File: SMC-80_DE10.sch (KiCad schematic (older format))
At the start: 19 parts, among them J1 IDE, J2 Port A, J3 Arduino1, J4 DE10-Lite GPIO, J5 Arduino2

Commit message: Renamed to SMC-80 DE10, new layout
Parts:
- C1: symbol de10-lite-ram-rom-ide-rescue:C_Small-Device-sbc_z80-rescue-THS-80-rescue-de10-lite-ram-rom-rescue -> SMC-80_DE10-rescue:C_Small-Device-sbc_z80-rescue-THS-80-rescue-de10-lite-ram-rom-rescue
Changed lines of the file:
@@
 NoConn ~ 2400 1250
 $Comp
-L de10-lite-ram-rom-ide-rescue:C_Small-Device-sbc_z80-rescue-THS-80-rescue-de10-lite-ram-rom-rescue C?
+L SMC-80_DE10-rescue:C_Small-Device-sbc_z80-rescue-THS-80-rescue-de10-lite-ram-rom-rescue C?
 U 1 1 5D65939B
 P 3300 2050
@@
 $EndComp
 $Comp
-L de10-lite-ram-rom-ide-rescue:GND-power-sbc_z80-rescue-THS-80-rescue-de10-lite-ram-rom-rescue #PWR06
+L SMC-80_DE10-rescue:GND-power-sbc_z80-rescue-THS-80-rescue-de10-lite-ram-rom-rescue #PWR06
 U 1 1 5D65A340
 P 3300 2150

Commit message: rotated layout
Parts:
- removed C1: 100nF, Capacitor_SMD:C_0603_1608Metric_Pad1.05x0.95mm_HandSolder, symbol SMC-80_DE10-rescue:C_Small-Device-sbc_z80-rescue-THS-80-rescue-de10-lite-ram-ro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
- removed D1: GRN, LED_SMD:LED_0603_1608Metric_Pad1.05x0.95mm_HandSolder, symbol Device:LED
- removed J1: IDE, Connector_PinHeader_2.54mm:PinHeader_2x20_P2.54mm_Horizontal, symbol Connector_Generic:Conn_02x20_Odd_Even
- removed J2: Port A, Connector_PinHeader_2.54mm:PinHeader_1x06_P2.54mm_Vertical, symbol Connector_Generic:Conn_01x06
- removed JP1: IDE PWR, Connector_PinHeader_2.54mm:PinHeader_1x02_P2.54mm_Vertical, symbol Device:Jumper_NC_Small
- removed R1, R2, R3, R4: 10K, Resistor_SMD:R_0603_1608Metric_Pad1.05x0.95mm_HandSolder, symbol Device:R_Small
- removed R5: 1K, Resistor_SMD:R_0603_1608Metric_Pad1.05x0.95mm_HandSolder, symbol Device:R_Small
- removed R6, R8: 100K, Resistor_SMD:R_0603_1608Metric_Pad1.05x0.95mm_HandSolder, symbol Device:R_Small
- removed RN1: 2K2, Resistor_SMD:R_Cat16-4, symbol Device:R_Pack04
- renumbered C2 to C1, D2 to D1, J3 to J1, J4 to J2, J5 to J3, R7 to R1
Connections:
- net labels removed: IDE_~CE~, RX, TX, ~ACTIVE, ~CTS, ~RTS
- wire segments 156 -> 88
- no-connect marks 22 -> 14
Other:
- note removed: "AB5"
- note removed: "AB6"
- note removed: "AB7"
- note removed: "AB8"
- note removed: "IDE Activity"
- moved on the sheet: C1, D1, J1, J2, J3, R1

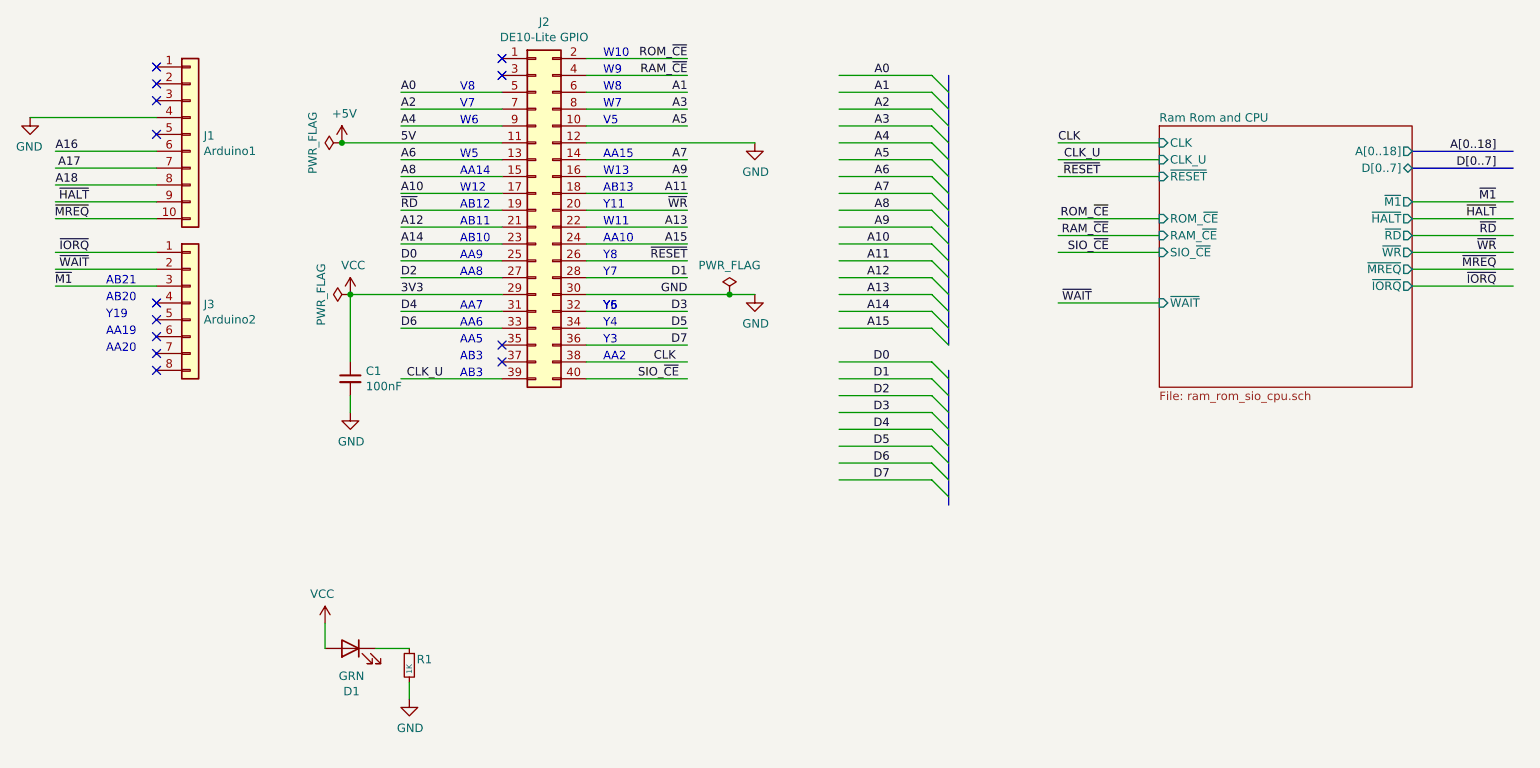
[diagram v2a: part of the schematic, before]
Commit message: Routing completed, fixed RAM/ROM paging
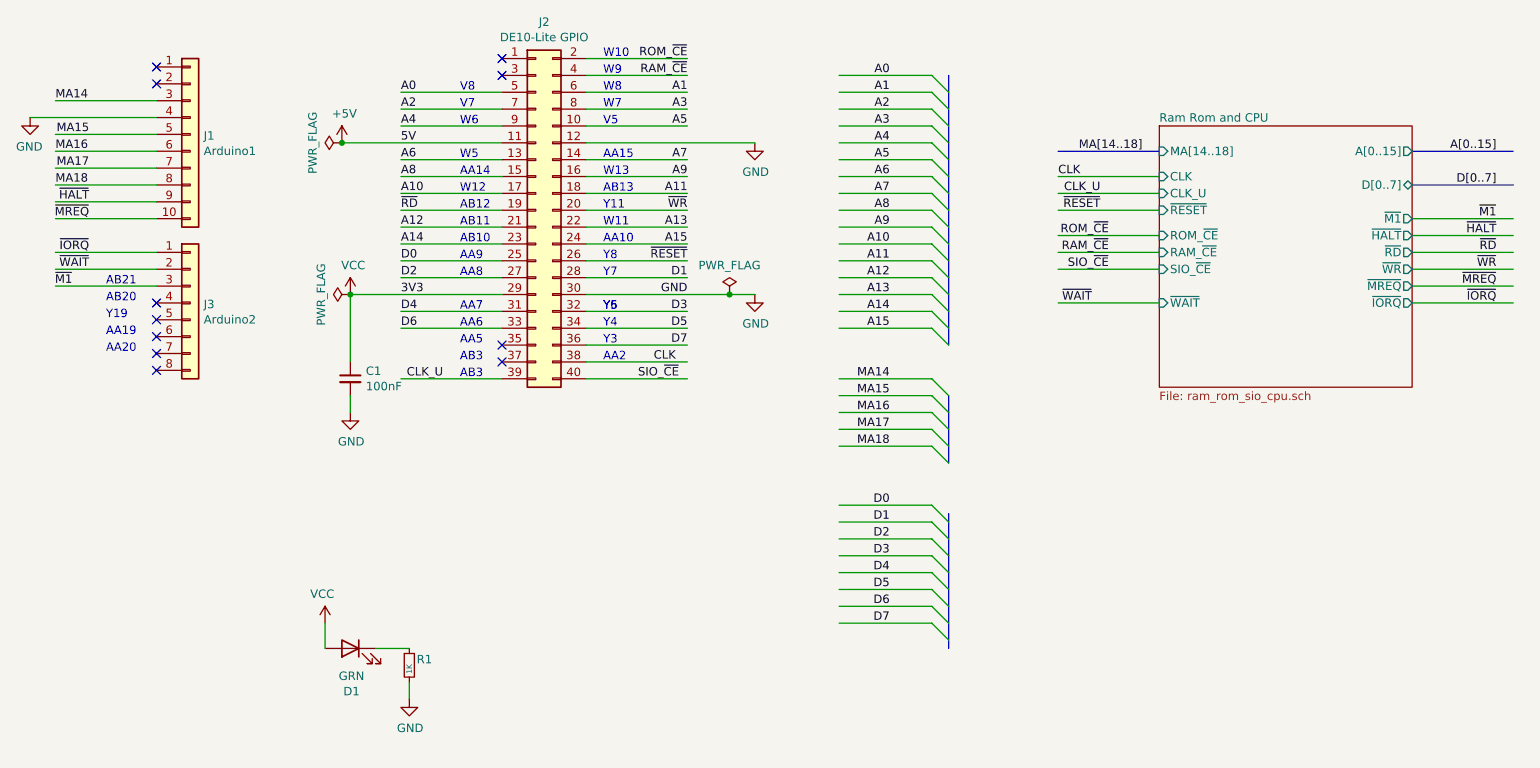
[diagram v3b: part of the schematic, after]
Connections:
- net labels added: A[0..15], MA14, MA15, MA16, MA17, MA18, MA[14..18]
- net labels removed: A16, A17, A18, A[0..18]
- wire segments 88 -> 95
- no-connect marks 14 -> 12
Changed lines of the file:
@@
 Wire Wire Line
 	1350 2350 750  2350
-NoConn ~ 1350 1350
 Wire Wire Line
 	600  1450 1350 1450
@@
 A14
 Text Label 750  1650 0    50   ~ 0
-A16
+MA16
 Text Label 750  1850 0    50   ~ 0
-A18
+MA18
 Text Label 2800 2100 0    50   ~ 0
 A12
@@
 Text Label 4500 2200 2    50   ~ 0
 A15
-Text Label 900  1750 2    50   ~ 0
-A17
+Text Label 950  1750 2    50   ~ 0
+MA17
 Text Notes 4000 2600 0    50   ~ 0
 Y6
@@
 F0 "Ram Rom and CPU" 50
 F1 "ram_rom_sio_cpu.sch" 50
-F2 "A[0..18]" O R 8800 1650 50
-F3 "D[0..7]" T R 8800 1750 50
-F4 "~M1" O R 8800 1950 50
-F5 "~MREQ" O R 8800 2350 50
-F6 "~IORQ" O R 8800 2450 50
-F7 "CLK" I L 7300 1600 50
-F8 "~RD" O R 8800 2150 50
-F9 "~WR" O R 8800 2250 50
-F10 "~WAIT" I L 7300 2550 50
-F11 "~HALT" O R 8800 2050 50
-F12 "RAM_~CE~" I L 7300 2150 50
-F13 "ROM_~CE~" I L 7300 2050 50
-F14 "SIO_~CE~" I L 7300 2250 50
-F15 "CLK_U" I L 7300 1700 50
-F16 "~RESET" I L 7300 1800 50
+F2 "D[0..7]" T R 8800 1850 50
+F3 "~M1" O R 8800 2050 50
+F4 "~MREQ" O R 8800 2450 50
+F5 "~IORQ" O R 8800 2550 50
+F6 "CLK" I L 7300 1800 50
+F7 "~RD" O R 8800 2250 50
+F8 "~WR" O R 8800 2350 50
+F9 "~WAIT" I L 7300 2550 50
+F10 "~HALT" O R 8800 2150 50
+F11 "RAM_~CE~" I L 7300 2250 50
+F12 "ROM_~CE~" I L 7300 2150 50
+F13 "SIO_~CE~" I L 7300 2350 50
+F14 "CLK_U" I L 7300 1900 50
+F15 "~RESET" I L 7300 2000 50
+F16 "A[0..15]" O R 8800 1650 50
+F17 "MA[14..18]" I L 7300 1650 50
 $EndSheet
 Wire Wire Line
-	6700 2050 7300 2050
-Text Label 7000 2050 2    50   ~ 0
+	6700 2150 7300 2150
+Text Label 7000 2150 2    50   ~ 0
 ROM_~CE
-Text Label 7000 2150 2    50   ~ 0
+Text Label 7000 2250 2    50   ~ 0
 RAM_~CE
 Wire Wire Line
-	6700 2150 7300 2150
-Wire Wire Line
 	6700 2250 7300 2250
-Text Label 9300 1950 2    50   ~ 0
+Wire Wire Line
+	6700 2350 7300 2350
+Text Label 9300 2050 2    50   ~ 0
 ~M1
 Wire Wire Line
-	9400 1950 8800 1950
+	9400 2050 8800 2050
 Wire Bus Line
 	8800 1650 9400 1650
 Text Label 9300 1650 2    50   ~ 0
-A[0..18]
+A[0..15]
 Wire Bus Line
-	8800 1750 9400 1750
-Text Label 9300 1750 2    50   ~ 0
+	8800 1850 9400 1850
+Text Label 9300 1850 2    50   ~ 0
 D[0..7]
 Wire Wire Line
-	9400 2050 8800 2050
-Text Label 9300 2050 2    50   ~ 0
+	9400 2150 8800 2150
+Text Label 9300 2150 2    50   ~ 0
 ~HALT
 Wire Wire Line
@@
 Text Label 6900 2550 2    50   ~ 0
 ~WAIT
-Text Label 7000 2250 2    50   ~ 0
+Text Label 7000 2350 2    50   ~ 0
 SIO_~CE
 Wire Wire Line
@@
 SIO_~CE
 Wire Wire Line
+	9400 2350 8800 2350
+Text Label 9300 2350 2    50   ~ 0
+~WR
+Text Label 9200 2250 0    50   ~ 0
+~RD
+Wire Wire Line
 	9400 2250 8800 2250
-Text Label 9300 2250 2    50   ~ 0
-~WR
-Text Label 9200 2150 0    50   ~ 0
-~RD
-Wire Wire Line
-	9400 2150 8800 2150
-Wire Wire Line
-	6700 1600 7300 1600
-Text Label 6700 1600 0    50   ~ 0
+Wire Wire Line
+	6700 1800 7300 1800
+Text Label 6700 1800 0    50   ~ 0
 CLK
-Text Label 6950 1800 2    50   ~ 0
+Text Label 6950 2000 2    50   ~ 0
 ~RESET
 Wire Wire Line
-	6700 1800 7300 1800
+	6700 2000 7300 2000
 Text Label 3050 3000 2    50   ~ 0
 CLK_U
 Wire Wire Line
 	3900 2900 4500 2900
-Text Label 6950 1700 2    50   ~ 0
+Text Label 6950 1900 2    50   ~ 0
 CLK_U
 Wire Wire Line
-	6700 1700 7300 1700
-Wire Wire Line
-	9400 2350 8800 2350
-Text Label 9300 2350 2    50   ~ 0
+	6700 1900 7300 1900
+Wire Wire Line
+	9400 2450 8800 2450
+Text Label 9300 2450 2    50   ~ 0
 ~MREQ
-Text Label 9300 2450 2    50   ~ 0
+Text Label 9300 2550 2    50   ~ 0
 ~IORQ
 Wire Wire Line
-	9400 2450 8800 2450
+	9400 2550 8800 2550
 Wire Wire Line
 	5400 1200 5950 1200
@@
 	5400 2700 5950 2700
 Wire Wire Line
-	5400 2900 5950 2900
-Wire Wire Line
-	5400 3000 5950 3000
-Wire Wire Line
-	5400 3100 5950 3100
-Wire Wire Line
-	5400 3200 5950 3200
-Wire Wire Line
-	5400 3300 5950 3300
-Wire Wire Line
-	5400 3400 5950 3400
-Wire Wire Line
-	5400 3500 5950 3500
-Wire Wire Line
-	5400 3600 5950 3600
+	5400 3750 5950 3750
+Wire Wire Line
+	5400 3850 5950 3850
+Wire Wire Line
+	5400 3950 5950 3950
+Wire Wire Line
+	5400 4050 5950 4050
+Wire Wire Line
+	5400 4150 5950 4150
+Wire Wire Line
+	5400 4250 5950 4250
+Wire Wire Line
+	5400 4350 5950 4350
+Wire Wire Line
+	5400 4450 5950 4450
 Text Label 5700 1200 2    50   ~ 0
 A0
@@
 Text Label 5700 2700 2    50   ~ 0
 A15
-Text Label 5700 2900 2    50   ~ 0
+Text Label 5700 3750 2    50   ~ 0
 D0
-Text Label 5700 3000 2    50   ~ 0
+Text Label 5700 3850 2    50   ~ 0
 D1
-Text Label 5700 3100 2    50   ~ 0
+Text Label 5700 3950 2    50   ~ 0
 D2
-Text Label 5700 3200 2    50   ~ 0
+Text Label 5700 4050 2    50   ~ 0
 D3
-Text Label 5700 3300 2    50   ~ 0
+Text Label 5700 4150 2    50   ~ 0
 D4
-Text Label 5700 3400 2    50   ~ 0
+Text Label 5700 4250 2    50   ~ 0
 D5
-Text Label 5700 3500 2    50   ~ 0
+Text Label 5700 4350 2    50   ~ 0
 D6
-Text Label 5700 3600 2    50   ~ 0
+Text Label 5700 4450 2    50   ~ 0
 D7
 Entry Wire Line
@@
 	5950 2700 6050 2800
 Entry Wire Line
-	5950 2900 6050 3000
-Entry Wire Line
-	5950 3000 6050 3100
-Entry Wire Line
-	5950 3100 6050 3200
-Entry Wire Line
-	5950 3200 6050 3300
-Entry Wire Line
-	5950 3300 6050 3400
-Entry Wire Line
-	5950 3400 6050 3500
-Entry Wire Line
-	5950 3500 6050 3600
-Entry Wire Line
-	5950 3600 6050 3700
+	5950 3750 6050 3850
+Entry Wire Line
+	5950 3850 6050 3950
+Entry Wire Line
+	5950 3950 6050 4050
+Entry Wire Line
+	5950 4050 6050 4150
+Entry Wire Line
+	5950 4150 6050 4250
+Entry Wire Line
+	5950 4250 6050 4350
+Entry Wire Line
+	5950 4350 6050 4450
+Entry Wire Line
+	5950 4450 6050 4550
 NoConn ~ 4850 5400
 NoConn ~ 1350 1250
@@
 	1    0    0    -1
 $EndComp
-NoConn ~ 1350 1550
 NoConn ~ 1350 2550
 NoConn ~ 1350 2650
@@
 NoConn ~ 3400 2900
 NoConn ~ 3400 2800
+Text Label 750  1350 0    50   ~ 0
+MA14
+Wire Wire Line
+	750  1350 1350 1350
+Wire Wire Line
+	1350 1550 750  1550
+Text Label 950  1550 2    50   ~ 0
+MA15
 Wire Bus Line
-	6050 2950 6050 3750
+	6700 1650 7300 1650
+Text Label 7200 1650 2    50   ~ 0
+MA[14..18]
+Wire Wire Line
+	5400 3000 5950 3000
+Wire Wire Line
+	5400 3100 5950 3100
+Wire Wire Line
+	5400 3200 5950 3200
+Wire Wire Line
+	5400 3300 5950 3300
+Wire Wire Line
+	5400 3400 5950 3400
+Text Label 5700 3000 2    50   ~ 0
+MA14
+Text Label 5700 3100 2    50   ~ 0
+MA15
+Text Label 5700 3200 2    50   ~ 0
+MA16
+Text Label 5700 3300 2    50   ~ 0
+MA17
+Text Label 5700 3400 2    50   ~ 0
+MA18
+Entry Wire Line
+	5950 3000 6050 3100
+Entry Wire Line
+	5950 3100 6050 3200
+Entry Wire Line
+	5950 3200 6050 3300
+Entry Wire Line
+	5950 3300 6050 3400
+Entry Wire Line
+	5950 3400 6050 3500
+Wire Bus Line
+	6050 3100 6050 3500
+Wire Bus Line
+	6050 3800 6050 4600
 Wire Bus Line
 	6050 1200 6050 2800

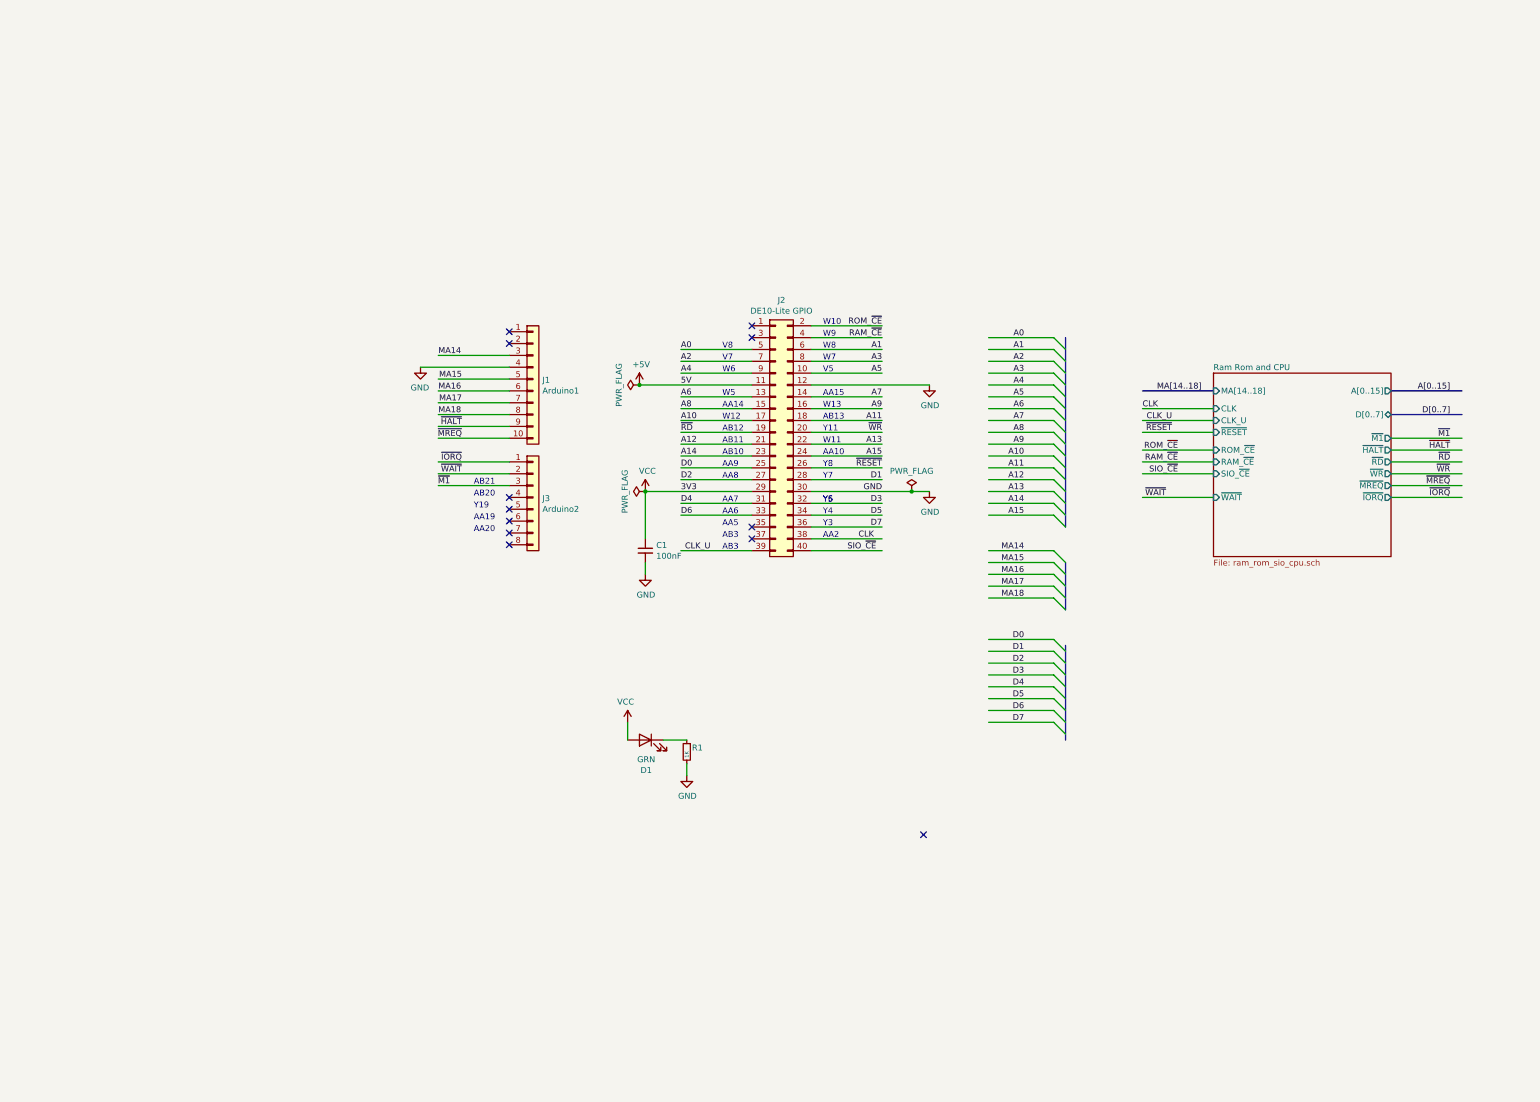
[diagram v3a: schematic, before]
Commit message: added gnd plane stitching
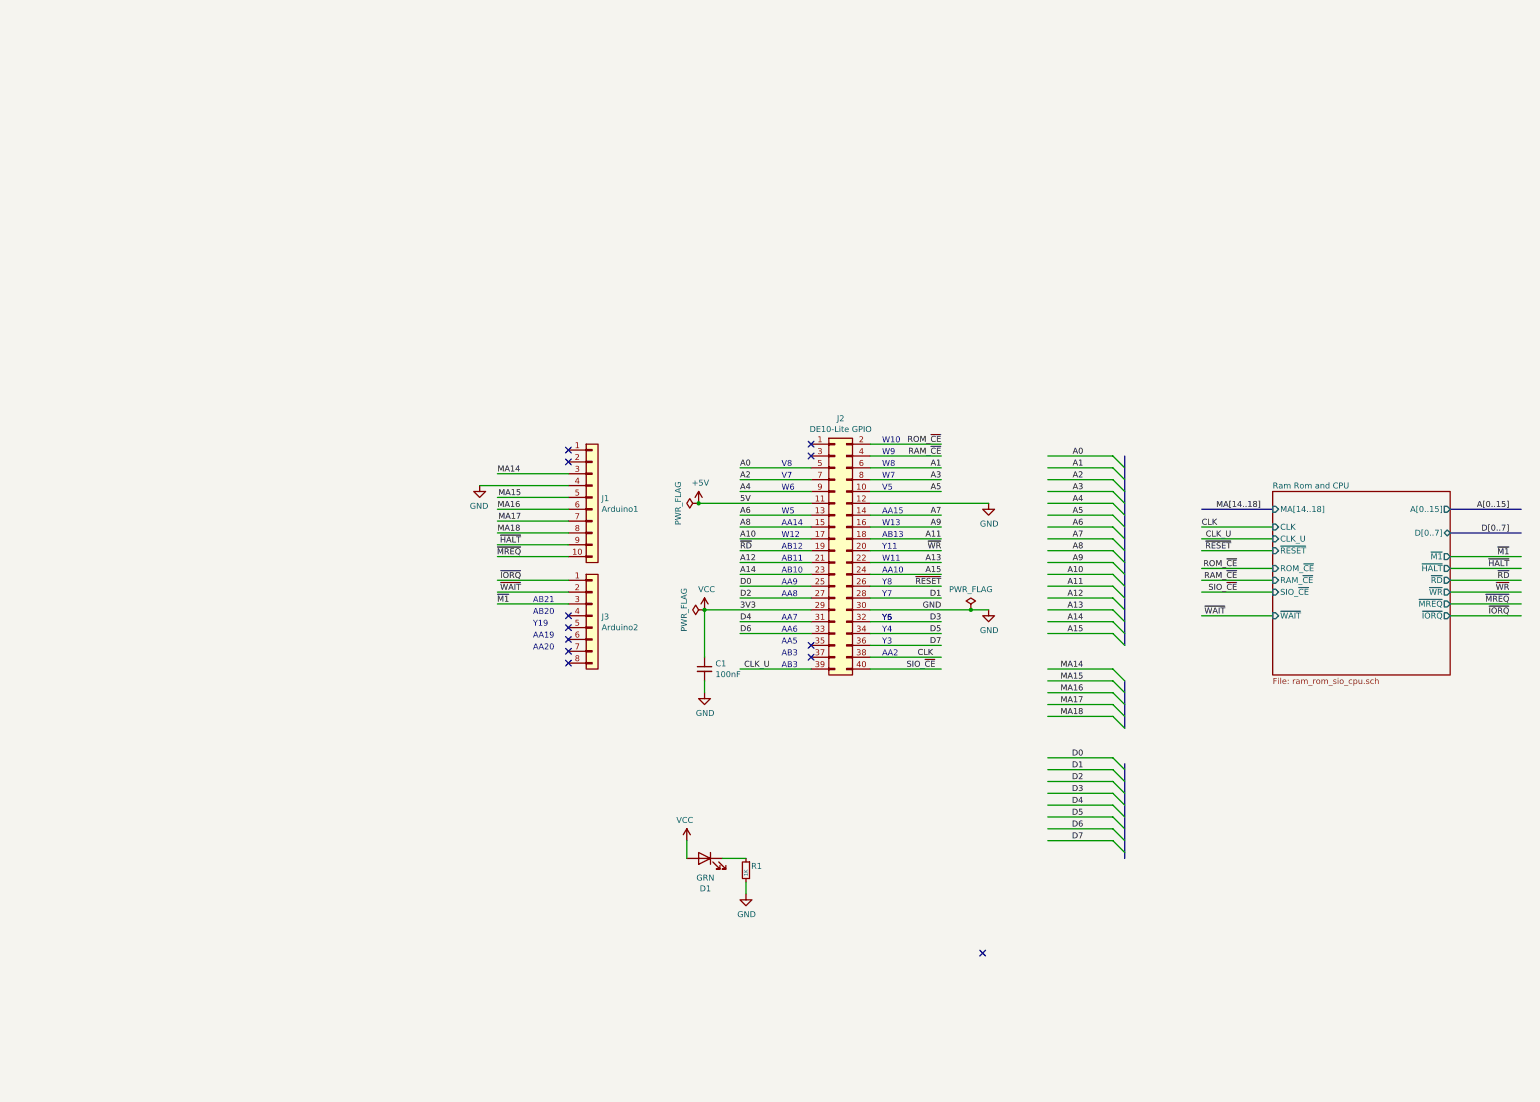
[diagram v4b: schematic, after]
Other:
- moved on the sheet: C1, D1, J1, J2, J3, R1
